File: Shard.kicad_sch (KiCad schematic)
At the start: 52 parts, among them J1 USB_C_Receptacle_USB2.0_16P, J2 Conn_01x08, J3 Conn_01x08, J4 Conn_01x08, J5 Conn_01x08, SW1 SW_Push, SW2 SW_Push, U1 ESP32-S3, U2 USBLC6-2P6, U3 TLV76733DRVx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

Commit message: Started routing USB & Power
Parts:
- R10, R6, R7, R8, R9: footprint Resistor_SMD:R_0603_1608Metric -> Resistor_SMD:R_01005_0402Metric; REF C177184 -> C270300
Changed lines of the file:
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@@
 			)
 		)
-		(property "Footprint" "Resistor_SMD:R_0603_1608Metric"
+		(property "Footprint" "Resistor_SMD:R_01005_0402Metric"
 			(at 203.2 53.848 90)
 			(effects
@@
 			)
 		)
-		(property "REF" " C177184"
+		(property "REF" " C270300"
 			(at 203.2 52.07 90)
 			(effects
@@
 			)
 		)
-		(property "Footprint" "Resistor_SMD:R_0603_1608Metric"
+		(property "Footprint" "Resistor_SMD:R_01005_0402Metric"
 			(at 203.2 43.688 90)
 			(effects
@@
 			)
 		)
-		(property "REF" " C177184"
+		(property "REF" " C270300"
 			(at 203.2 41.91 90)
 			(effects
@@
 			)
 		)
-		(property "Footprint" "Resistor_SMD:R_0603_1608Metric"
+		(property "Footprint" "Resistor_SMD:R_01005_0402Metric"
 			(at 203.2 51.308 90)
 			(effects
@@
 			)
 		)
-		(property "REF" " C177184"
+		(property "REF" " C270300"
 			(at 203.2 49.53 90)
 			(effects
@@
 			)
 		)
-		(property "Footprint" "Resistor_SMD:R_0603_1608Metric"
+		(property "Footprint" "Resistor_SMD:R_01005_0402Metric"
 			(at 203.2 48.768 90)
 			(effects
@@
 			)
 		)
-		(property "REF" " C177184"
+		(property "REF" " C270300"
 			(at 203.2 46.99 90)
 			(effects
@@
 			)
 		)
-		(property "Footprint" "Resistor_SMD:R_0603_1608Metric"
+		(property "Footprint" "Resistor_SMD:R_01005_0402Metric"
 			(at 203.2 41.148 90)
 			(effects
@@
 			)
 		)
-		(property "REF" " C177184"
+		(property "REF" " C270300"
 			(at 203.2 39.37 90)
 			(effects

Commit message: Completed Power routing
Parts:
- C6: footprint Capacitor_SMD:C_0201_0603Metric -> Capacitor_SMD:C_0402_1005Metric; REF C5209398 -> C325464
- C7, C8: footprint Capacitor_SMD:C_0201_0603Metric -> Capacitor_SMD:C_0402_1005Metric; REF C312124 -> C312123
- D4: footprint LED_SMD:LED_WS2812B_PLCC4_5.0x5.0mm_P3.2mm -> LED_SMD:LED_WS2812B-2020_PLCC4_2.0x2.0mm; REF C2843785 -> C965555
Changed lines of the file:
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@@
 			)
 		)
-		(property "Footprint" "Capacitor_SMD:C_0201_0603Metric"
+		(property "Footprint" "Capacitor_SMD:C_0402_1005Metric"
 			(at 75.8952 160.02 0)
 			(effects
@@
 			)
 		)
-		(property "REF" " C5209398"
+		(property "REF" " C325464"
 			(at 74.93 156.21 0)
 			(effects
@@
 			)
 		)
-		(property "Footprint" "Capacitor_SMD:C_0201_0603Metric"
+		(property "Footprint" "Capacitor_SMD:C_0402_1005Metric"
 			(at 87.3252 160.02 0)
 			(effects
@@
 			)
 		)
-		(property "REF" " C312124"
+		(property "REF" "C312123"
 			(at 86.36 156.21 0)
 			(effects
@@
 			)
 		)
-		(property "Footprint" "LED_SMD:LED_WS2812B_PLCC4_5.0x5.0mm_P3.2mm"
+		(property "Footprint" "LED_SMD:LED_WS2812B-2020_PLCC4_2.0x2.0mm"
 			(at 201.93 154.94 0)
 			(effects
@@
 			)
 		)
-		(property "REF" " C2843785"
+		(property "REF" "C965555"
 			(at 200.66 147.32 0)
 			(effects
@@
 			)
 		)
-		(property "Footprint" "Capacitor_SMD:C_0201_0603Metric"
+		(property "Footprint" "Capacitor_SMD:C_0402_1005Metric"
 			(at 102.5652 160.02 0)
 			(effects
@@
 			)
 		)
-		(property "REF" " C312124"
+		(property "REF" "C312123"
 			(at 101.6 156.21 0)
 			(effects

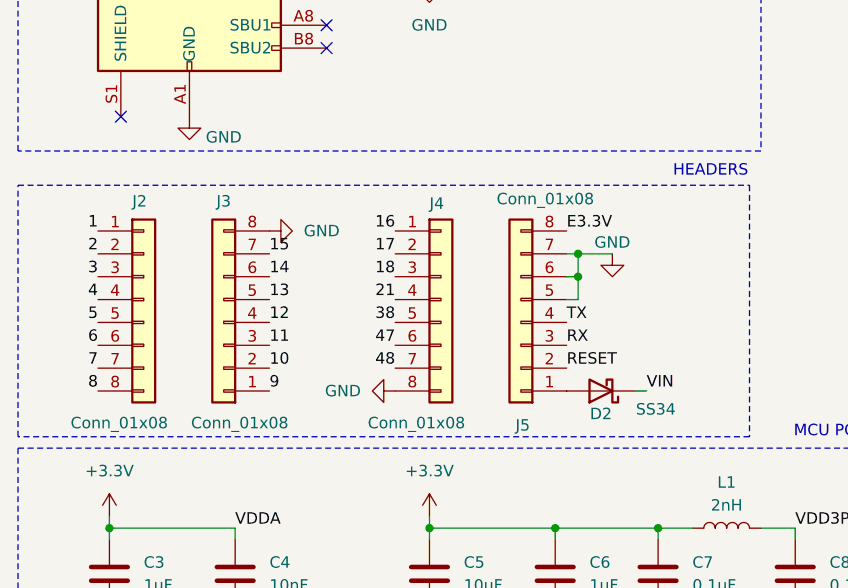
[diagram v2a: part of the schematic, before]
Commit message: Routed most GPIO pins
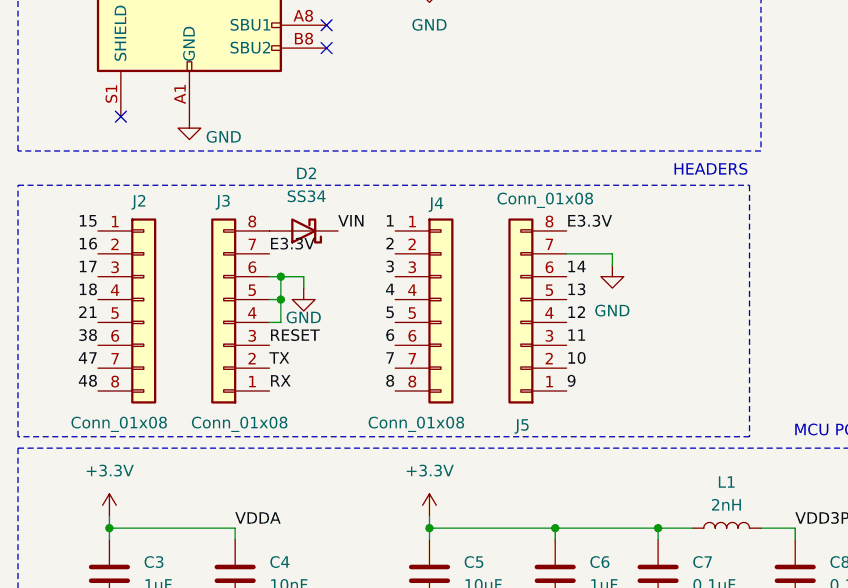
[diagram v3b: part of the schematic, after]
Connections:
- net 1: now also J4.1 (Pin_1); no longer J2.1 (Pin_1)
- net 10: now also J5.2 (Pin_2); no longer J3.2 (Pin_2)
- net 11: now also J5.3 (Pin_3); no longer J3.3 (Pin_3)
- net 12: now also J5.4 (Pin_4); no longer J3.4 (Pin_4)
- net 13: now also J5.5 (Pin_5); no longer J3.5 (Pin_5)
- net 14: now also J5.6 (Pin_6); no longer J3.6 (Pin_6)
- net 15: now also J2.1 (Pin_1); no longer J3.7 (Pin_7)
- net 16: now also J2.2 (Pin_2); no longer J4.1 (Pin_1)
- net 17: now also J2.3 (Pin_3); no longer J4.2 (Pin_2)
- net 18: now also J2.4 (Pin_4); no longer J4.3 (Pin_3)
- net 2: now also J4.2 (Pin_2); no longer J2.2 (Pin_2)
- net 21: now also J2.5 (Pin_5); no longer J4.4 (Pin_4)
- net 3: now also J4.3 (Pin_3); no longer J2.3 (Pin_3)
- net 38: now also J2.6 (Pin_6); no longer J4.5 (Pin_5)
- net 4: now also J4.4 (Pin_4); no longer J2.4 (Pin_4)
- net 47: now also J2.7 (Pin_7); no longer J4.6 (Pin_6)
- net 48: now also J2.8 (Pin_8); no longer J4.7 (Pin_7)
- net 5: now also J4.5 (Pin_5); no longer J2.5 (Pin_5)
- net 6: now also J4.6 (Pin_6); no longer J2.6 (Pin_6)
- net 7: now also J4.7 (Pin_7); no longer J2.7 (Pin_7)
- net 8: now also J4.8 (Pin_8); no longer J2.8 (Pin_8)
- net 9: now also J5.1 (Pin_1); no longer J3.1 (Pin_1)
- net E3.3V: now also J3.7 (Pin_7)
- net GND: now also J3.4 (Pin_4), J3.5 (Pin_5), J3.6 (Pin_6); no longer J3.8 (Pin_8), J4.8 (Pin_8), J5.5 (Pin_5), J5.6 (Pin_6)
- net RESET: now also J3.3 (Pin_3); no longer J5.2 (Pin_2)
- net RX: now also J3.1 (Pin_1); no longer J5.3 (Pin_3)
- net TX: now also J3.2 (Pin_2); no longer J5.4 (Pin_4)
- net at D2.2 (A): now also J3.8 (Pin_8); no longer J5.1 (Pin_1)

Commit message: Finished routing
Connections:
- net +3.3V: no longer R4.1
- net 21: no longer J2.5 (Pin_5)
- net E3.3V: now also J5.7 (Pin_7), R4.1; no longer J5.8 (Pin_8)
- net GND: now also J2.5 (Pin_5), J5.8 (Pin_8); no longer J5.7 (Pin_7)
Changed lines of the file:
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@@
 	(wire
 		(pts
-			(xy 81.28 120.65) (xy 81.28 121.92)
+			(xy 82.55 118.11) (xy 82.55 119.38)
 		)
 		(stroke
@@
 	(wire
 		(pts
-			(xy 76.2 120.65) (xy 81.28 120.65)
-		)
-		(stroke
-			(width 0)
-			(type default)
-		)
-	)
-	(wire
-		(pts
 			(xy 236.22 134.62) (xy 242.57 134.62)
 		)
@@
 	(wire
 		(pts
+			(xy 19.05 128.27) (xy 19.05 129.54)
+		)
+		(stroke
+			(width 0)
+			(type default)
+		)
+	)
+	(wire
+		(pts
 			(xy 240.03 123.19) (xy 236.22 123.19)
 		)
@@
 	(wire
 		(pts
+			(xy 24.13 128.27) (xy 19.05 128.27)
+		)
+		(stroke
+			(width 0)
+			(type default)
+		)
+	)
+	(wire
+		(pts
 			(xy 68.58 34.29) (xy 68.58 36.83)
 		)
@@
 	(wire
 		(pts
+			(xy 76.2 118.11) (xy 82.55 118.11)
+		)
+		(stroke
+			(width 0)
+			(type default)
+		)
+	)
+	(wire
+		(pts
 			(xy 241.3 49.53) (xy 241.3 50.8)
 		)
@@
 	)
 	(label "E3.3V"
-		(at 76.2 118.11 0)
+		(at 76.2 120.65 0)
 		(fields_autoplaced yes)
 		(effects
@@
 		)
 	)
-	(label "21"
-		(at 24.13 128.27 180)
-		(fields_autoplaced yes)
-		(effects
-			(font
-				(size 1.27 1.27)
-			)
-			(justify right bottom)
-		)
-	)
 	(label "SPIQ"
 		(at 236.22 139.7 180)
@@
 		)
 	)
+	(label "E3.3V"
+		(at 144.78 146.05 0)
+		(fields_autoplaced yes)
+		(effects
+			(font
+				(size 1.27 1.27)
+			)
+			(justify left bottom)
+		)
+	)
 	(label "SPICLK"
 		(at 236.22 134.62 180)
@@
 	)
 	(symbol
-		(lib_id "power:+3.3V")
-		(at 144.78 146.05 0)
-		(unit 1)
-		(exclude_from_sim no)
-		(in_bom yes)
-		(on_board yes)
-		(dnp no)
-		(property "Reference" "#PWR028"
-			(at 144.78 149.86 0)
-			(effects
-				(font
-					(size 1.27 1.27)
-				)
-				(hide yes)
-			)
-		)
-		(property "Value" "+3.3V"
-			(at 149.352 144.272 0)
-			(effects
-				(font
-					(size 1.27 1.27)
-				)
-			)
-		)
-		(property "Footprint" ""
-			(at 144.78 146.05 0)
-			(effects
-				(font
-					(size 1.27 1.27)
-				)
-				(hide yes)
-			)
-		)
-		(property "Datasheet" ""
-			(at 144.78 146.05 0)
-			(effects
-				(font
-					(size 1.27 1.27)
-				)
-				(hide yes)
-			)
-		)
-		(property "Description" "Power symbol creates a global label with name \"+3.3V\""
-			(at 144.78 146.05 0)
-			(effects
-				(font
-					(size 1.27 1.27)
-				)
-				(hide yes)
-			)
-		)
-		(pin "1"
-		)
-		(instances
-			(project ""
-				(path "/3c105ee6-b3fb-4e5c-8d42-ae0480f22c07"
-					(reference "#PWR028")
-					(unit 1)
-				)
-			)
-		)
-	)
-	(symbol
 		(lib_id "Device:C")
 		(at 90.17 29.21 0)
@@
 	)
 	(symbol
+		(lib_id "power:GND")
+		(at 19.05 129.54 0)
+		(unit 1)
+		(exclude_from_sim no)
+		(in_bom yes)
+		(on_board yes)
+		(dnp no)
+		(property "Reference" "#PWR028"
+			(at 19.05 135.89 0)
+			(effects
+				(font
+					(size 1.27 1.27)
+				)
+				(hide yes)
+			)
+		)
+		(property "Value" "GND"
+			(at 19.05 132.842 0)
+			(effects
+				(font
+					(size 1.27 1.27)
+				)
+			)
+		)
+		(property "Footprint" ""
+			(at 19.05 129.54 0)
+			(effects
+				(font
+					(size 1.27 1.27)
+				)
+				(hide yes)
+			)
+		)
+		(property "Datasheet" ""
+			(at 19.05 129.54 0)
+			(effects
+				(font
+					(size 1.27 1.27)
+				)
+				(hide yes)
+			)
+		)
+		(property "Description" "Power symbol creates a global label with name \"GND\" , ground"
+			(at 19.05 129.54 0)
+			(effects
+				(font
+					(size 1.27 1.27)
+				)
+				(hide yes)
+			)
+		)
+		(pin "1"
+		)
+		(instances
+			(project "Shard"
+				(path "/3c105ee6-b3fb-4e5c-8d42-ae0480f22c07"
+					(reference "#PWR028")
+					(unit 1)
+				)
+			)
+		)
+	)
+	(symbol
 		(lib_id "Device:C")
 		(at 262.89 83.82 0)
@@
 	(symbol
 		(lib_id "power:GND")
-		(at 81.28 121.92 0)
+		(at 82.55 119.38 0)
 		(unit 1)
 		(exclude_from_sim no)
@@
 		(fields_autoplaced yes)
 		(property "Reference" "#PWR035"
-			(at 81.28 128.27 0)
+			(at 82.55 125.73 0)
 			(effects
 				(font
@@
 		)
 		(property "Value" "GND"
-			(at 81.28 127 0)
+			(at 82.55 124.46 0)
 			(effects
 				(font
@@
 		)
 		(property "Footprint" ""
-			(at 81.28 121.92 0)
+			(at 82.55 119.38 0)
 			(effects
 				(font
@@
 		)
 		(property "Datasheet" ""
-			(at 81.28 121.92 0)
+			(at 82.55 119.38 0)
 			(effects
 				(font
@@
 		)
 		(property "Description" "Power symbol creates a global label with name \"GND\" , ground"
-			(at 81.28 121.92 0)
+			(at 82.55 119.38 0)
 			(effects
 				(font

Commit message: Add stitching vias, checked DRC rules
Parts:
- U1: REF C2913194 -> C2913194
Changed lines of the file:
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@@
 			)
 		)
-		(property "REF" "C2913194"
+		(property "REF" " C2913194"
 			(at 172.72 67.31 0)
 			(effects

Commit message: Add production files
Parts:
- U1: REF C2913194 -> C2913194
- renumbered SW2 to BOOT, SW1 to RESET
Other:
- company: (none) -> Enderlab
- title: (none) -> Shard

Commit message: Fixed some things
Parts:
- R10, R6, R7, R8, R9: footprint Resistor_SMD:R_01005_0402Metric -> Resistor_SMD:R_0201_0603Metric; REF C270300 -> C965347
- R12: REF C185685 -> C17722
- renumbered BOOT to BOOT1, RESET to RESET1
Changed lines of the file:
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@@
 			)
 		)
-		(property "Footprint" "Resistor_SMD:R_01005_0402Metric"
+		(property "Footprint" "Resistor_SMD:R_0201_0603Metric"
 			(at 203.2 53.848 90)
 			(effects
@@
 			)
 		)
-		(property "REF" " C270300"
+		(property "REF" "C965347"
 			(at 203.2 52.07 90)
 			(effects
@@
 			)
 		)
-		(property "REF" "C185685"
+		(property "REF" " C17722"
 			(at 204.47 85.09 90)
 			(effects
@@
 			)
 		)
-		(property "Footprint" "Resistor_SMD:R_01005_0402Metric"
+		(property "Footprint" "Resistor_SMD:R_0201_0603Metric"
 			(at 203.2 43.688 90)
 			(effects
@@
 			)
 		)
-		(property "REF" " C270300"
+		(property "REF" "C965347"
 			(at 203.2 41.91 90)
 			(effects
@@
 			)
 		)
-		(property "Footprint" "Resistor_SMD:R_01005_0402Metric"
+		(property "Footprint" "Resistor_SMD:R_0201_0603Metric"
 			(at 203.2 51.308 90)
 			(effects
@@
 			)
 		)
-		(property "REF" " C270300"
+		(property "REF" "C965347"
 			(at 203.2 49.53 90)
 			(effects
@@
 			)
 		)
-		(property "Footprint" "Resistor_SMD:R_01005_0402Metric"
+		(property "Footprint" "Resistor_SMD:R_0201_0603Metric"
 			(at 203.2 48.768 90)
 			(effects
@@
 			)
 		)
-		(property "REF" " C270300"
+		(property "REF" "C965347"
 			(at 203.2 46.99 90)
 			(effects
@@
 		(dnp no)
 		(fields_autoplaced yes)
-		(property "Reference" "BOOT"
+		(property "Reference" "BOOT1"
 			(at 135.89 175.26 0)
 			(effects
@@
 			(project "Shard"
 				(path "/3c105ee6-b3fb-4e5c-8d42-ae0480f22c07"
-					(reference "BOOT")
+					(reference "BOOT1")
 					(unit 1)
 				)
@@
 		(dnp no)
 		(fields_autoplaced yes)
-		(property "Reference" "RESET"
+		(property "Reference" "RESET1"
 			(at 135.89 149.86 0)
 			(effects
@@
 			(project ""
 				(path "/3c105ee6-b3fb-4e5c-8d42-ae0480f22c07"
-					(reference "RESET")
+					(reference "RESET1")
 					(unit 1)
 				)
@@
 			)
 		)
-		(property "Footprint" "Resistor_SMD:R_01005_0402Metric"
+		(property "Footprint" "Resistor_SMD:R_0201_0603Metric"
 			(at 203.2 41.148 90)
 			(effects
@@
 			)
 		)
-		(property "REF" " C270300"
+		(property "REF" "C965347"
 			(at 203.2 39.37 90)
 			(effects

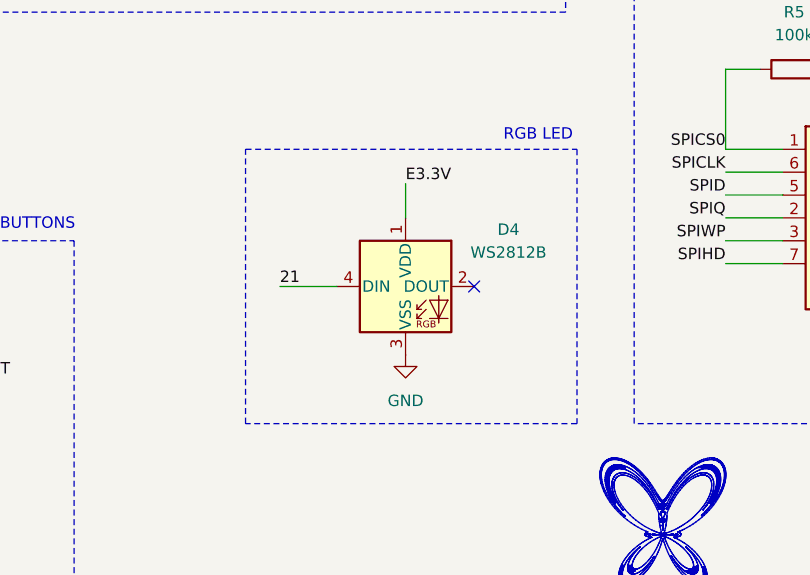
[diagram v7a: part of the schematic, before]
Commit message: Fix design errors & update README
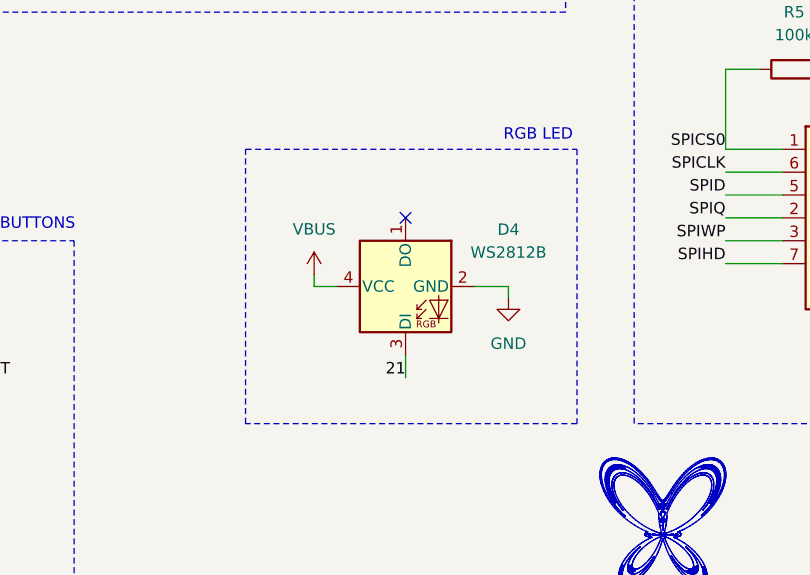
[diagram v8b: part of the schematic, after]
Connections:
- net 21: now also D4.3 (DI); no longer D4.4 (DIN)
- net E3.3V: no longer D4.1 (VDD)
- net GND: now also D4.2 (GND); no longer D4.3 (VSS)
- net VBUS: now also D4.4 (VCC)
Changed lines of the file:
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@@
 	)
 	(no_connect
+		(at 200.66 139.7)
+	)
+	(no_connect
 		(at 49.53 95.25)
 	)
@@
 		(at 49.53 97.79)
 	)
-	(no_connect
-		(at 208.28 147.32)
-	)
 	(wire
 		(pts
@@
 	(wire
 		(pts
+			(xy 212.09 147.32) (xy 208.28 147.32)
+		)
+		(stroke
+			(width 0)
+			(type default)
+		)
+	)
+	(wire
+		(pts
 			(xy 43.18 125.73) (xy 44.45 125.73)
 		)
@@
 	(wire
 		(pts
-			(xy 200.66 135.89) (xy 200.66 139.7)
-		)
-		(stroke
-			(width 0)
-			(type default)
-		)
-	)
-	(wire
-		(pts
 			(xy 195.58 97.79) (xy 203.2 97.79)
 		)
@@
 	(wire
 		(pts
-			(xy 186.69 147.32) (xy 193.04 147.32)
-		)
-		(stroke
-			(width 0)
-			(type default)
-		)
-	)
-	(wire
-		(pts
 			(xy 207.01 39.37) (xy 212.09 39.37)
 		)
@@
 	(wire
 		(pts
+			(xy 190.5 147.32) (xy 193.04 147.32)
+		)
+		(stroke
+			(width 0)
+			(type default)
+		)
+	)
+	(wire
+		(pts
 			(xy 255.27 40.64) (xy 261.62 40.64)
 		)
@@
 	(wire
 		(pts
+			(xy 212.09 148.59) (xy 212.09 147.32)
+		)
+		(stroke
+			(width 0)
+			(type default)
+		)
+	)
+	(wire
+		(pts
+			(xy 190.5 146.05) (xy 190.5 147.32)
+		)
+		(stroke
+			(width 0)
+			(type default)
+		)
+	)
+	(wire
+		(pts
 			(xy 130.81 182.88) (xy 125.73 182.88)
 		)
@@
 	(wire
 		(pts
+			(xy 200.66 154.94) (xy 200.66 157.48)
+		)
+		(stroke
+			(width 0)
+			(type default)
+		)
+	)
+	(wire
+		(pts
 			(xy 232.41 44.45) (xy 233.68 44.45)
 		)
@@
 	)
 	(label "E3.3V"
-		(at 200.66 135.89 0)
-		(fields_autoplaced yes)
-		(effects
-			(font
-				(size 1.27 1.27)
-			)
-			(justify left bottom)
-		)
-	)
-	(label "E3.3V"
 		(at 76.2 120.65 0)
 		(fields_autoplaced yes)
@@
 		)
 	)
-	(label "21"
-		(at 186.69 147.32 0)
-		(fields_autoplaced yes)
-		(effects
-			(font
-				(size 1.27 1.27)
-			)
-			(justify left bottom)
-		)
-	)
 	(label "XTAL_N"
 		(at 144.78 97.79 180)
@@
 		)
 	)
+	(label "21"
+		(at 200.66 157.48 180)
+		(fields_autoplaced yes)
+		(effects
+			(font
+				(size 1.27 1.27)
+			)
+			(justify right bottom)
+		)
+	)
 	(label "TX"
 		(at 43.18 133.35 0)
@@
 	)
 	(symbol
+		(lib_id "power:GND")
+		(at 212.09 148.59 0)
+		(unit 1)
+		(exclude_from_sim no)
+		(in_bom yes)
+		(on_board yes)
+		(dnp no)
+		(fields_autoplaced yes)
+		(property "Reference" "#PWR034"
+			(at 212.09 154.94 0)
+			(effects
+				(font
+					(size 1.27 1.27)
+				)
+				(hide yes)
+			)
+		)
+		(property "Value" "GND"
+			(at 212.09 153.67 0)
+			(effects
+				(font
+					(size 1.27 1.27)
+				)
+			)
+		)
+		(property "Footprint" ""
+			(at 212.09 148.59 0)
+			(effects
+				(font
+					(size 1.27 1.27)
+				)
+				(hide yes)
+			)
+		)
+		(property "Datasheet" ""
+			(at 212.09 148.59 0)
+			(effects
+				(font
+					(size 1.27 1.27)
+				)
+				(hide yes)
+			)
+		)
+		(property "Description" "Power symbol creates a global label with name \"GND\" , ground"
+			(at 212.09 148.59 0)
+			(effects
+				(font
+					(size 1.27 1.27)
+				)
+				(hide yes)
+			)
+		)
+		(pin "1"
+		)
+		(instances
+			(project ""
+				(path "/3c105ee6-b3fb-4e5c-8d42-ae0480f22c07"
+					(reference "#PWR034")
+					(unit 1)
+				)
+			)
+		)
+	)
+	(symbol
 		(lib_id "Device:C")
 		(at 90.17 29.21 0)
@@
 		)
 		(property "Description" "RGB LED with integrated controller"
-			(at 200.66 147.32 0)
+			(at 200.914 149.86 0)
 			(effects
 				(font
@@
 	(symbol
 		(lib_id "power:GND")
-		(at 200.66 154.94 0)
-		(unit 1)
-		(exclude_from_sim no)
-		(in_bom yes)
-		(on_board yes)
-		(dnp no)
-		(fields_autoplaced yes)
-		(property "Reference" "#PWR034"
-			(at 200.66 161.29 0)
-			(effects
-				(font
-					(size 1.27 1.27)
-				)
-				(hide yes)
-			)
-		)
-		(property "Value" "GND"
-			(at 200.66 160.02 0)
-			(effects
-				(font
-					(size 1.27 1.27)
-				)
-			)
-		)
-		(property "Footprint" ""
-			(at 200.66 154.94 0)
-			(effects
-				(font
-					(size 1.27 1.27)
-				)
-				(hide yes)
-			)
-		)
-		(property "Datasheet" ""
-			(at 200.66 154.94 0)
-			(effects
-				(font
-					(size 1.27 1.27)
-				)
-				(hide yes)
-			)
-		)
-		(property "Description" "Power symbol creates a global label with name \"GND\" , ground"
-			(at 200.66 154.94 0)
-			(effects
-				(font
-					(size 1.27 1.27)
-				)
-				(hide yes)
-			)
-		)
-		(pin "1"
-		)
-		(instances
-			(project ""
-				(path "/3c105ee6-b3fb-4e5c-8d42-ae0480f22c07"
-					(reference "#PWR034")
-					(unit 1)
-				)
-			)
-		)
-	)
-	(symbol
-		(lib_id "power:GND")
 		(at 34.29 105.41 0)
 		(unit 1)
@@
 					(unit 1)
 				)
+			)
+		)
+	)
+	(symbol
+		(lib_id "power:VBUS")
+		(at 190.5 146.05 0)
+		(unit 1)
+		(exclude_from_sim no)
+		(in_bom yes)
+		(on_board yes)
+		(dnp no)
+		(fields_autoplaced yes)
+		(property "Reference" "#PWR036"
+			(at 190.5 149.86 0)
+			(effects
+				(font
+					(size 1.27 1.27)
+				)
+				(hide yes)
+			)
+		)
+		(property "Value" "VBUS"
+			(at 190.5 140.97 0)
+			(effects
+				(font
+					(size 1.27 1.27)
+				)
+			)
+		)
+		(property "Footprint" ""
+			(at 190.5 146.05 0)
+			(effects
+				(font
+					(size 1.27 1.27)
+				)
+				(hide yes)
+			)
+		)
+		(property "Datasheet" ""
+			(at 190.5 146.05 0)
+			(effects
+				(font
+					(size 1.27 1.27)
+				)
+				(hide yes)
+			)
+		)
+		(property "Description" "Power symbol creates a global label with name \"VBUS\""
+			(at 190.5 146.05 0)
+			(effects
+				(font
+					(size 1.27 1.27)
+				)
+				(hide yes)
+			)
+		)
+		(pin "1"
+		)
+		(instances
+			(project "Shard"
+				(path "/3c105ee6-b3fb-4e5c-8d42-ae0480f22c07"
+					(reference "#PWR036")
+					(unit 1)
+				)
